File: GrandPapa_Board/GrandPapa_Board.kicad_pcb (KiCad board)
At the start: 2 copper layers, 82 x 82 mm, 0 parts

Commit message: add footprints, group layouts
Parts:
- added C1: 10uF, Capacitor_SMD:C_0805_2012Metric_Pad1.18x1.45mm_HandSolder, F.Cu at (253.8, 90.2)
- added C10: 4.7uF, Capacitor_SMD:C_0805_2012Metric_Pad1.18x1.45mm_HandSolder, F.Cu at (252.1, 25.6)
- added C11: 4.7uF, Capacitor_SMD:C_0805_2012Metric_Pad1.18x1.45mm_HandSolder, F.Cu at (260.4, 31.9)
- added C12: 0.1uF, Capacitor_SMD:C_0805_2012Metric_Pad1.18x1.45mm_HandSolder, F.Cu at (244.1, 21.0)
- added C13: 0.1uF, Capacitor_SMD:C_0805_2012Metric_Pad1.18x1.45mm_HandSolder, F.Cu at (60.6, 121.7)
- added C14: 0.1uF, Capacitor_SMD:C_0805_2012Metric_Pad1.18x1.45mm_HandSolder, F.Cu at (253.8, 77.5)
- added C15: 44 uF, Capacitor_SMD:C_0805_2012Metric_Pad1.18x1.45mm_HandSolder, F.Cu at (266.5, 94.0)
- added C16: 27pF, Capacitor_SMD:C_0805_2012Metric_Pad1.18x1.45mm_HandSolder, F.Cu at (155.8, 19.1)
- added C17: 27pF, Capacitor_SMD:C_0805_2012Metric_Pad1.18x1.45mm_HandSolder, F.Cu at (155.8, 24.0)
- added C18: 0.1uF 20V, Capacitor_SMD:C_0805_2012Metric_Pad1.18x1.45mm_HandSolder, F.Cu at (175.0, 24.8)
- added C19: 0.1uF 20V, Capacitor_SMD:C_0805_2012Metric_Pad1.18x1.45mm_HandSolder, F.Cu at (182.6, 34.7)
- added C2: 10uF, Capacitor_SMD:C_0805_2012Metric_Pad1.18x1.45mm_HandSolder, F.Cu at (41.0, 128.9)
- added C21: 0.1uF, Capacitor_SMD:C_0805_2012Metric_Pad1.18x1.45mm_HandSolder, F.Cu at (53.6, 34.9)
- added C22: 10uF, Capacitor_SMD:C_0805_2012Metric_Pad1.18x1.45mm_HandSolder, B.Cu at (25.4, 41.3)
- added C23: 10uF, Capacitor_SMD:C_0805_2012Metric_Pad1.18x1.45mm_HandSolder, F.Cu at (182.4, 31.1)
- added C3: 0.1uF, Capacitor_SMD:C_0805_2012Metric_Pad1.18x1.45mm_HandSolder, F.Cu at (253.8, 87.1)
- added C4: 5nF, Capacitor_SMD:C_0805_2012Metric_Pad1.18x1.45mm_HandSolder, F.Cu at (256.8, 103.5)
- added C5: 10uF, Capacitor_SMD:C_0805_2012Metric_Pad1.18x1.45mm_HandSolder, F.Cu at (44.5, 119.5)
- added C6: 0.1uF, Capacitor_SMD:C_0805_2012Metric_Pad1.18x1.45mm_HandSolder, F.Cu at (259.9, 94.0)
- added C7: 4.7uF, Capacitor_SMD:C_0805_2012Metric_Pad1.18x1.45mm_HandSolder, F.Cu at (50.5, 124.3)
- added C8: 25pF, Capacitor_SMD:C_0805_2012Metric_Pad1.18x1.45mm_HandSolder, F.Cu at (252.2, 103.6)
- added C9: 4.7uF, Capacitor_SMD:C_0805_2012Metric_Pad1.18x1.45mm_HandSolder, F.Cu at (255.3, 25.6)
- added D1: 150120BS75000, LED_SMD:LED_1206_3216Metric_Pad1.42x1.75mm_HandSolder, F.Cu at (240.6, 156.3)
- added D3: QBLP650-IW, LED_SMD:LED_1206_3216Metric_Pad1.42x1.75mm_HandSolder, F.Cu at (187.6, 44.5)
- added D4: 156120RS75000, LED_SMD:LED_1206_3216Metric_Pad1.42x1.75mm_HandSolder, F.Cu at (187.4, 40.6)
- added D5: 150120BS75000, LED_SMD:LED_1206_3216Metric_Pad1.42x1.75mm_HandSolder, F.Cu at (187.5, 36.8)
- added D6: QBLP650-IW, LED_SMD:LED_1206_3216Metric_Pad1.42x1.75mm_HandSolder, F.Cu at (250.8, 43.8)
- added D7: 156120RS75000, LED_SMD:LED_1206_3216Metric_Pad1.42x1.75mm_HandSolder, F.Cu at (253.4, 44.0)
- added D8: 150120BS75000, LED_SMD:LED_1206_3216Metric_Pad1.42x1.75mm_HandSolder, F.Cu at (248.3, 44.0)
- added F1: 1.2A, Fuse:Fuse_0805_2012Metric_Pad1.15x1.40mm_HandSolder, F.Cu at (248.0, 87.0)
- added F2: 1.2A, Fuse:Fuse_0805_2012Metric_Pad1.15x1.40mm_HandSolder, F.Cu at (27.6, 128.9)
- added F3: 1.2A, Fuse:Fuse_0805_2012Metric_Pad1.15x1.40mm_HandSolder, F.Cu at (260.4, 29.8)
- added H1: MountingHole_Pad, MountingHole:MountingHole_3.5mm_Pad_Via, F.Cu at (22.9, 165.1)
- added H2: MountingHole_Pad, MountingHole:MountingHole_3.5mm_Pad_Via, F.Cu at (36.8, 167.6)
- added H3: MountingHole_Pad, MountingHole:MountingHole_3.5mm_Pad_Via, F.Cu at (118.1, 137.2)
- added H4: MountingHole_Pad, MountingHole:MountingHole_3.5mm_Pad_Via, F.Cu at (40.6, 186.1)
- added H5: MountingHole_Pad, MountingHole:MountingHole_3.5mm_Pad_Via, F.Cu at (24.1, 177.8)
- added H6: MountingHole_Pad, MountingHole:MountingHole_3.5mm_Pad_Via, F.Cu at (190.5, 65.4)
- added H7: MountingHole_Pad, MountingHole:MountingHole_3.5mm_Pad_Via, F.Cu at (190.5, 137.8)
- added H8: MountingHole_Pad, MountingHole:MountingHole_3.5mm_Pad_Via, F.Cu at (118.1, 64.8)
- added J1: 3.7V LiPo Single Cell, Connector_JST:JST_PH_S2B-PH-K_1x02_P2.00mm_Horizontal, F.Cu at (266.8, 31.5)
- added J11: Dupont 01x04_Male, Connector_PinHeader_2.54mm:PinHeader_1x04_P2.54mm_Vertical, F.Cu at (54.0, 174.6)
- added J2: HARWIN_ROCKET, PapaOld:connector_Harwin_M80-5000642, F.Cu at (196.6, 29.8)
- added J3: Dupont 02x03_Female, PapaOld:PinHeader_2x03_P2.00mm_Vertical_MINISENSOR_Harwin_Spacing, F.Cu at (120.0, 82.5)
- added J4: HARWIN_MINISENSOR, PapaOld:connector_Harwin_M80-5000642, F.Cu at (43.1, 26.7)
- added J5: Dupont 01x06_Female, PapaOld:PinHeader_2x03_P2.00mm_Vertical_MINISENSOR_Harwin_Spacing, F.Cu at (181.3, 115.6)
- added J6: Conn_02x06, Connector_PinHeader_2.54mm:PinHeader_1x05_P2.54mm_Vertical, F.Cu at (182.2, 21.0)
- added J7: HARWIN_KALMAN, PapaOld:connector_Harwin_M80-5000642, F.Cu at (42.9, 32.4)
- added L1: 5.6uH, Inductor_SMD:L_Vishay_IHLP-2020, F.Cu at (263.4, 99.1)
- added L2: 4.7uH, Inductor_SMD:L_Sumida_CDMC6D28_7.25x6.5mm, F.Cu at (33.0, 123.2)
- added R1: 20mR, Resistor_SMD:R_1206_3216Metric_Pad1.30x1.75mm_HandSolder, F.Cu at (248.2, 84.5)
- added R10: 0, Resistor_SMD:R_0805_2012Metric_Pad1.20x1.40mm_HandSolder, F.Cu at (50.4, 121.9)
- added R11: 10kR, Resistor_SMD:R_0805_2012Metric_Pad1.20x1.40mm_HandSolder, F.Cu at (168.0, 19.7)
- added R12: 100R, Resistor_SMD:R_0805_2012Metric_Pad1.20x1.40mm_HandSolder, F.Cu at (167.0, 24.1)
- added R13: 100R, Resistor_SMD:R_0805_2012Metric_Pad1.20x1.40mm_HandSolder, F.Cu at (182.4, 44.5)
- added R14: 150R, Resistor_SMD:R_0805_2012Metric_Pad1.20x1.40mm_HandSolder, F.Cu at (182.3, 40.6)
- added R15: 100R, Resistor_SMD:R_0805_2012Metric_Pad1.20x1.40mm_HandSolder, F.Cu at (182.6, 36.8)
- added R16: 11kR, Resistor_SMD:R_0805_2012Metric_Pad1.20x1.40mm_HandSolder, F.Cu at (256.9, 106.0)
- added R17: 10kR, Resistor_SMD:R_0805_2012Metric_Pad1.20x1.40mm_HandSolder, F.Cu at (53.6, 40.0)
- added R18: 10kR, Resistor_SMD:R_0805_2012Metric_Pad1.20x1.40mm_HandSolder, F.Cu at (53.6, 37.5)
- added R19: 70kR, Resistor_SMD:R_0805_2012Metric_Pad1.20x1.40mm_HandSolder, F.Cu at (248.3, 99.1)
- added R2: 1MR, Resistor_SMD:R_0805_2012Metric_Pad1.20x1.40mm_HandSolder, F.Cu at (47.0, 122.8)
- added R20: 470R, Resistor_SMD:R_0805_2012Metric_Pad1.20x1.40mm_HandSolder, F.Cu at (253.4, 37.2)
- added R21: 470R, Resistor_SMD:R_0805_2012Metric_Pad1.20x1.40mm_HandSolder, F.Cu at (248.3, 37.2)
- added R22: 0, Resistor_SMD:R_0805_2012Metric_Pad1.20x1.40mm_HandSolder, F.Cu at (248.6, 29.2)
- added R23: 20mR, Resistor_SMD:R_1206_3216Metric_Pad1.30x1.75mm_HandSolder, F.Cu at (243.6, 29.2)
- added R24: 0, Resistor_SMD:R_0805_2012Metric_Pad1.20x1.40mm_HandSolder, F.Cu at (248.6, 26.7)
- added R25: 324kR, Resistor_SMD:R_0805_2012Metric_Pad1.20x1.40mm_HandSolder, F.Cu at (252.2, 106.0)
- added R26: 10kR, Resistor_SMD:R_0805_2012Metric_Pad1.20x1.40mm_HandSolder, F.Cu at (36.7, 45.1)
- added R27: 15k, Resistor_SMD:R_0805_2012Metric_Pad1.20x1.40mm_HandSolder, F.Cu at (259.3, 84.5)
- added R3: 100R, Resistor_SMD:R_0805_2012Metric_Pad1.20x1.40mm_HandSolder, F.Cu at (245.4, 156.2)
- added R4: 2kR, Resistor_SMD:R_0805_2012Metric_Pad1.20x1.40mm_HandSolder, F.Cu at (258.4, 37.1)
- added R5: 25kR, Resistor_SMD:R_0805_2012Metric_Pad1.20x1.40mm_HandSolder, F.Cu at (255.9, 37.1)
- added R6: 470R, Resistor_SMD:R_0805_2012Metric_Pad1.20x1.40mm_HandSolder, F.Cu at (250.8, 37.2)
- added R7: 500R, Resistor_SMD:R_0805_2012Metric_Pad1.20x1.40mm_HandSolder, F.Cu at (60.6, 123.8)
- added R8: 10k, Resistor_SMD:R_0805_2012Metric_Pad1.20x1.40mm_HandSolder, F.Cu at (259.4, 87.6)
- added R9: 0, Resistor_SMD:R_0805_2012Metric_Pad1.20x1.40mm_HandSolder, F.Cu at (253.8, 84.5)
- added TH1: 10k, Resistor_SMD:R_0805_2012Metric_Pad1.20x1.40mm_HandSolder, F.Cu at (248.6, 33.7)
- added TP1: TestPoint, Connector_PinHeader_2.54mm:PinHeader_1x01_P2.54mm_Vertical, F.Cu at (258.4, 45.1)
- added TP2: TestPoint, Connector_PinHeader_2.54mm:PinHeader_1x01_P2.54mm_Vertical, F.Cu at (238.1, 21.3)
- added TP3: TestPoint, Connector_PinHeader_2.54mm:PinHeader_1x01_P2.54mm_Vertical, F.Cu at (55.9, 128.3)
- added TP4: TestPoint, Connector_PinHeader_2.54mm:PinHeader_1x01_P2.54mm_Vertical, F.Cu at (259.5, 75.6)
- added TP5: TestPoint, Connector_PinHeader_2.54mm:PinHeader_1x01_P2.54mm_Vertical, F.Cu at (248.9, 19.7)
- added TP6: TestPoint, Connector_PinHeader_2.54mm:PinHeader_1x01_P2.54mm_Vertical, F.Cu at (22.2, 128.9)
- added TP7: TestPoint, Connector_PinHeader_2.54mm:PinHeader_1x01_P2.54mm_Vertical, F.Cu at (190.5, 17.1)
- added U1: MCP1642B-50I/MS, Package_SO:MSOP-8_3x3mm_P0.65mm, F.Cu at (41.2, 122.9)
- added U10: MCP2515-I/P, Package_SO:SOIC-18W_7.5x11.6mm_P1.27mm, F.Cu at (45.1, 42.5)
- added U2: BD9E302EFJ, Package_SO:HTSOP-8-1EP_3.9x4.9mm_P1.27mm_EP2.4x3.2mm, F.Cu at (254.3, 96.6)
- added U3: MCP73871T-1CCI/ML, Package_DFN_QFN:QFN-20-1EP_4x4mm_P0.5mm_EP2.5x2.5mm, F.Cu at (254.0, 31.1)
- added U4: INA180, Package_TO_SOT_SMD:SOT-23-5_HandSoldering, F.Cu at (243.9, 26.0)
- added U5: FPF2124, Package_TO_SOT_SMD:SOT-23-5_HandSoldering, F.Cu at (55.5, 122.8)
- added U6: INA180, Package_TO_SOT_SMD:SOT-23-5_HandSoldering, F.Cu at (248.4, 78.5)
- added U7: MCP2562-E/SN, Package_SO:SOIC-8_3.9x4.9mm_P1.27mm, B.Cu at (31.5, 39.4)
- added U8: MCP2562-E/SN, Package_SO:SOIC-8_3.9x4.9mm_P1.27mm, F.Cu at (189.2, 30.5)
- added U9: PIC18F26K83, Package_SO:SSOP-28_5.3x10.2mm_P0.65mm, F.Cu at (172.7, 33.0)
- added Y1: 12MHz, Crystal:Crystal_HC49-4H_Vertical, F.Cu at (160.7, 19.1)
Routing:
- net Net-(C2-Pad1): track 0.00 -> 29.8 mm
- net Net-(C16-Pad1): track 0.00 -> 26.1 mm
- net Net-(C17-Pad1): track 0.00 -> 21.5 mm
- net /MCU and CAN Controllers/~{MCLR}: track 0.00 -> 13.2 mm
- net +5V: track 0.00 -> 12.5 mm
- net Net-(C1-Pad1): track 0.00 -> 12.3 mm
- net /MCU and CAN Controllers/ICSPCLK: track 0.00 -> 12.0 mm
- net Net-(L2-Pad2): track 0.00 -> 11.7 mm
- net Net-(R13-Pad1): track 0.00 -> 11.6 mm
- net /MCU and CAN Controllers/ICSPDAT: track 0.00 -> 10.4 mm
- net Net-(C6-Pad1): track 0.00 -> 9.93 mm
- net Net-(R1-Pad1): track 0.00 -> 8.16 mm
- net Net-(R14-Pad1): track 0.00 -> 8.08 mm
- net /Battery Charging/VBATT_VOLT_SENSE: track 0.00 -> 7.42 mm
- net Net-(C10-Pad1): track 0.00 -> 7.40 mm
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
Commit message: change stackup, mounting holes, connector footprints, power reg layout, fuse values
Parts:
- J2, J7: moved to B.Cu
- J3, J5: footprint PapaOld:PinHeader_2x03_P2.00mm_Vertical_MINISENSOR_Harwin_Spacing -> PapaOld:connector_Harwin_M80-5000642
- R27: value 15k -> 15kR
- R8: value 10k -> 10kR
- moved TP4 237.3 mm to (37.9, 160.5)
- moved R8 231.7 mm to (42.5, 169.1)
- moved R27 231.4 mm to (42.5, 165.7), turned to 180 degrees
- moved C8 229.5 mm to (39.7, 190.3), turned to 90 degrees
- moved R16 226.4 mm to (45.2, 186.3), turned to 90 degrees
- moved L1 226.3 mm to (53.4, 183.5)
- moved C4 225.6 mm to (45.2, 181.7), turned to 90 degrees
- moved R19 225.2 mm to (42.4, 190.3), turned to -90 degrees
- moved R25 225.2 mm to (41.5, 185.4)
- moved C15 225.1 mm to (59.5, 182.4), turned to 90 degrees
- moved C6 225.0 mm to (51.0, 177.3), turned to 90 degrees
- moved U2 223.0 mm to (45.8, 175.6)
- moved C3 222.1 mm to (47.4, 169.2), turned to 0 degrees
- moved R9 221.7 mm to (45.2, 159.5), turned to -90 degrees
- moved C1 219.9 mm to (47.3, 165.7), turned to 0 degrees
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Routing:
- net Net-(C2-Pad1): track 29.8 -> 0.00 mm
- net Net-(C16-Pad1): track 26.1 -> 10.4 mm
- net Net-(C1-Pad1): track 12.3 -> 0.00 mm
- net Net-(L2-Pad2): track 11.7 -> 0.00 mm
- net Net-(R13-Pad1): track 11.6 -> 0.00 mm
- net Net-(C17-Pad1): track 21.5 -> 10.4 mm
- net Net-(C6-Pad1): track 9.93 -> 0.00 mm
- net Net-(R14-Pad1): track 8.08 -> 0.00 mm
- net Net-(R4-Pad1): track 6.38 -> 0.60 mm
- net Net-(R5-Pad1): track 5.80 -> 0.46 mm
- net Net-(C7-Pad1): track 5.17 -> 0.00 mm
- net Net-(R15-Pad1): track 5.93 -> 1.12 mm
- net +5V: track 12.5 -> 8.11 mm
- net Net-(R23-Pad1): track 0.00 -> 4.24 mm
- net Net-(R22-Pad2): track 0.00 -> 4.22 mm
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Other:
- outline, holes or cut-outs redrawn
- copper layers 2 -> 4
- board text added: "5V_ALWAYS"
- board text added: "GPS"
- board text added: "KALMAN"
- board text added: "LOGGER"
- board text added: "MINISENSOR"
- board text added: "ROCKETCAN"

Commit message: 4 straight hours of traces
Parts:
- removed TP6: TestPoint, Connector_PinHeader_2.54mm:PinHeader_1x01_P2.54mm_Vertical
- C12, C13, C2, C21, C5, C7, F2, J1, R10, R17, R18, R2, R23, R24, R26, R7, TH1, U1, U10, U4, U5: moved to B.Cu
- C22, J7, U7: moved to F.Cu
- F1, F3: value 1.2A -> 1.5A
- moved J1 138.8 mm to (171.8, 132.8)
- moved C22 132.1 mm to (193.7, 102.0), turned to -90 degrees
- moved TP1 129.0 mm to (147.9, 111.7)
- moved F2 126.7 mm to (157.3, 134.1), turned to 180 degrees
- moved TP4 126.5 mm to (147.4, 97.2)
- moved L1 124.5 mm to (150.0, 104.8)
- moved U7 121.0 mm to (188.7, 97.3), turned to 0 degrees
- moved C3 120.1 mm to (139.6, 92.1)
- moved C1 119.8 mm to (139.6, 89.3)
- moved C2 119.0 mm to (153.4, 133.1)
- moved R19 118.6 mm to (132.7, 113.5)
- moved C6 118.2 mm to (141.2, 101.0)
- moved R27 118.2 mm to (132.8, 89.4)
- moved R8 118.2 mm to (132.7, 92.8)
- moved U2 118.2 mm to (136.0, 99.3)
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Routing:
- net /Power Supplies & Regulators/5V_SWITCHED: track 0.00 -> 205.5 mm
- net /CANH_PAYLOAD: track 0.00 -> 166.3 mm
- net /CANL_PAYLOAD: track 0.00 -> 156.4 mm
- net /Battery Charging/BATT_CHARGER_PG: track 0.00 -> 86.7 mm, vias 0 -> 2
- net /MCU and CAN Controllers/CANH_ROCKET: track 0.00 -> 79.5 mm, vias 0 -> 1
- net +5V: track 8.11 -> 86.2 mm, vias 0 -> 11
- net /Battery Charging/VBATT_CURR_SENSE: track 0.00 -> 74.4 mm, vias 0 -> 1
- net /Battery Charging/BATT_CHARGE_COMPLETE: track 0.00 -> 73.8 mm, vias 0 -> 2
- net /MCU and CAN Controllers/CANL_ROCKET: track 0.00 -> 73.1 mm, vias 0 -> 1
- net /Battery Charging/LOW_BAT: track 0.00 -> 69.4 mm, vias 0 -> 2
- net /MCU and CAN Controllers/12V_PWR_DIS: track 0.00 -> 64.7 mm, vias 0 -> 2
- net +BATT: track 0.00 -> 63.8 mm
- net +4.5V: track 0.00 -> 58.6 mm, vias 0 -> 6
- net /Battery Charging/VBATT_VOLT_SENSE: track 7.42 -> 63.2 mm, vias 0 -> 2
- net GND: track 0.00 -> 55.4 mm, vias 0 -> 8
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- added copper zone on In1.Cu, net +4.5V
- added copper zone on In1.Cu, net +5V
- added copper zone on B.Cu, net GND
- added copper zone on F.Cu, net GND
- added copper zone on In2.Cu, net GND

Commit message: update layout + routing
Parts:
- C1, C10, C11, C14, C15, C3, C4, C6, C8, C9, F1, F3, L1, L2, R1, R16, R19, R22, R25, R27, R4, R5, R8, R9, TP1, TP3, TP4, TP5, U2, U3, U6: moved to B.Cu
- moved R7 68.9 mm to (183.7, 118.3), turned to 0 degrees
- moved C13 63.5 mm to (176.0, 117.2), turned to 90 degrees
- moved U5 62.6 mm to (179.5, 116.9), turned to -90 degrees
- moved C7 56.2 mm to (179.6, 112.6), turned to 0 degrees
- moved F2 48.1 mm to (183.6, 93.8), turned to -90 degrees
- moved TP3 47.8 mm to (167.8, 105.6), turned to 180 degrees
- moved R10 47.3 mm to (170.8, 108.3), turned to -90 degrees
- moved C2 41.2 mm to (178.5, 100.4), turned to -90 degrees
- moved L2 39.6 mm to (175.8, 94.4)
- moved R2 39.5 mm to (174.2, 107.4)
- moved C5 39.2 mm to (170.9, 102.7)
- moved U1 39.2 mm to (174.7, 101.6)
- moved C10 29.5 mm to (148.2, 122.3), turned to -90 degrees
- moved TP4 27.2 mm to (140.5, 70.9), turned to 180 degrees
- moved F3 24.4 mm to (158.6, 119.3)
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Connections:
- J2 pad 4: /MCU and CAN Controllers/CANL_ROCKET -> /MCU and CAN Controllers/CANH_ROCKET
- J2 pad 5: /MCU and CAN Controllers/CANH_ROCKET -> /MCU and CAN Controllers/CANL_ROCKET
- J4 pad 4: /CANL_PAYLOAD -> /CANH_PAYLOAD
- J4 pad 5: /CANH_PAYLOAD -> /CANL_PAYLOAD
- J7 pad 4: /CANL_PAYLOAD -> /CANH_PAYLOAD
- J7 pad 5: /CANH_PAYLOAD -> /CANL_PAYLOAD
- TP3 pad 1: Net-(C7-Pad1) -> +5V
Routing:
- net /Power Supplies & Regulators/5V_SWITCHED: track 205.5 -> 0.02 mm, vias 0 -> 4
- net +5V: track 86.2 -> 40.8 mm, vias 11 -> 15
- net Net-(TH1-Pad1): track 3.28 -> 43.3 mm, vias 1 -> 2
- net /MCU and CAN Controllers/AUX_PWR_EN: track 18.0 -> 57.9 mm, vias 1 -> 3
- net /MCU and CAN Controllers/CANH_ROCKET: track 79.5 -> 45.5 mm
- net /Battery Charging/VBATT_CURR_SENSE: track 74.4 -> 40.9 mm, vias 1 -> 3
- net /CANL_PAYLOAD: track 156.4 -> 185.9 mm, vias 0 -> 5
- net +BATT: track 63.8 -> 37.0 mm, vias 0 -> 2
- net /MCU and CAN Controllers/CANL_ROCKET: track 73.1 -> 46.3 mm
- net Net-(F3-Pad1): track 37.2 -> 11.4 mm, vias 1 -> 0
- net Net-(C1-Pad1): track 44.4 -> 19.8 mm, vias 1 -> 0
- net /CANH_PAYLOAD: track 166.3 -> 189.4 mm, vias 0 -> 5
- net /MCU and CAN Controllers/12V_PWR_DIS: track 64.7 -> 45.2 mm, vias 2 -> 3
- net +12V: track 16.1 -> 0.00 mm
- net /MCU and CAN Controllers/CAN_INT: track 43.3 -> 27.3 mm, vias 1 -> 3
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- added copper zone on B.Cu, net +12V
- added copper zone on B.Cu, net +4.5V
- added copper zone on B.Cu, net +5V
- added copper zone on B.Cu, net /Battery Charging/VBATT_VOLT_SENSE
- added copper zone on B.Cu, net /Power Supplies & Regulators/5V_SWITCHED
- added copper zone on In1.Cu, net /Power Supplies & Regulators/5V_SWITCHED
- added copper zone on B.Cu, net Net-(C1-Pad1)
- added copper zone on B.Cu, net Net-(C2-Pad1)
- added copper zone on B.Cu, net Net-(C6-Pad1)
- added copper zone on B.Cu, net Net-(L2-Pad2)
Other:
- outline, holes or cut-outs redrawn
- board text removed: "5V_ALWAYS"

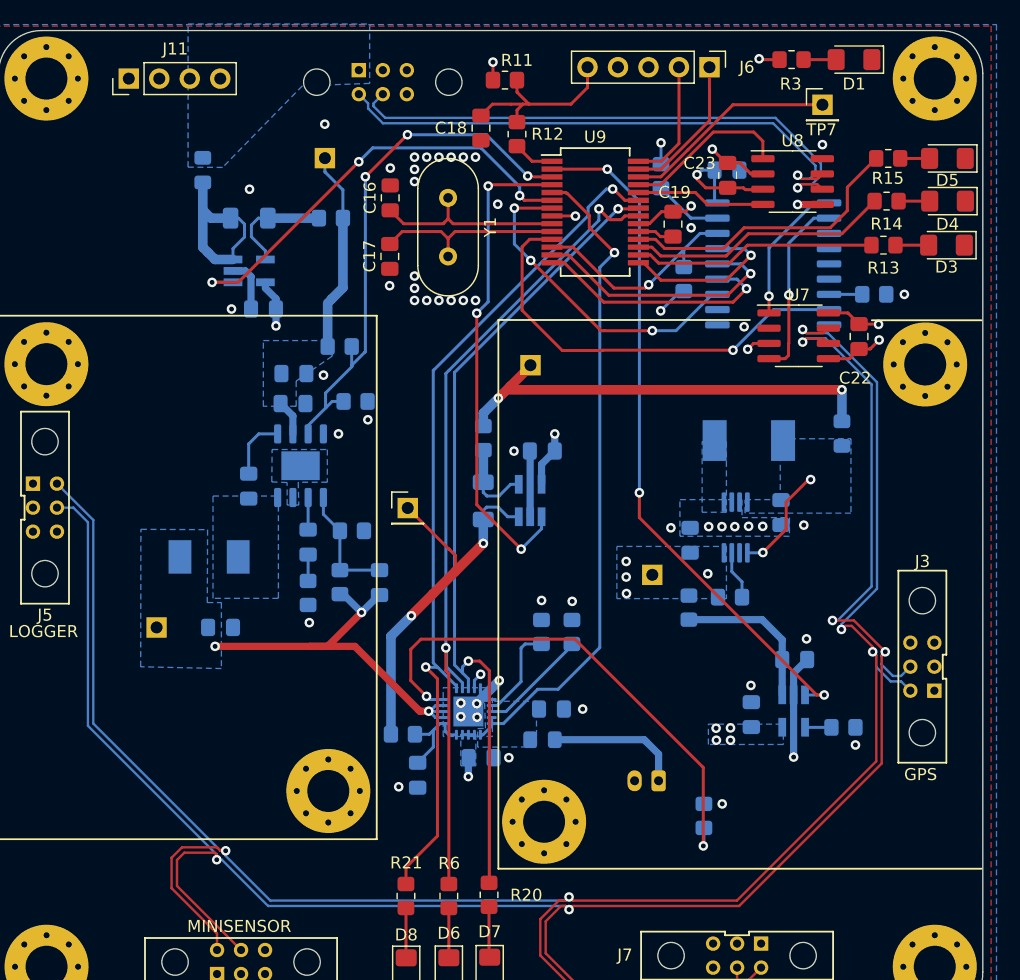
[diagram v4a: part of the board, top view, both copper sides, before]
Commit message: Fix silkscreen; add logo
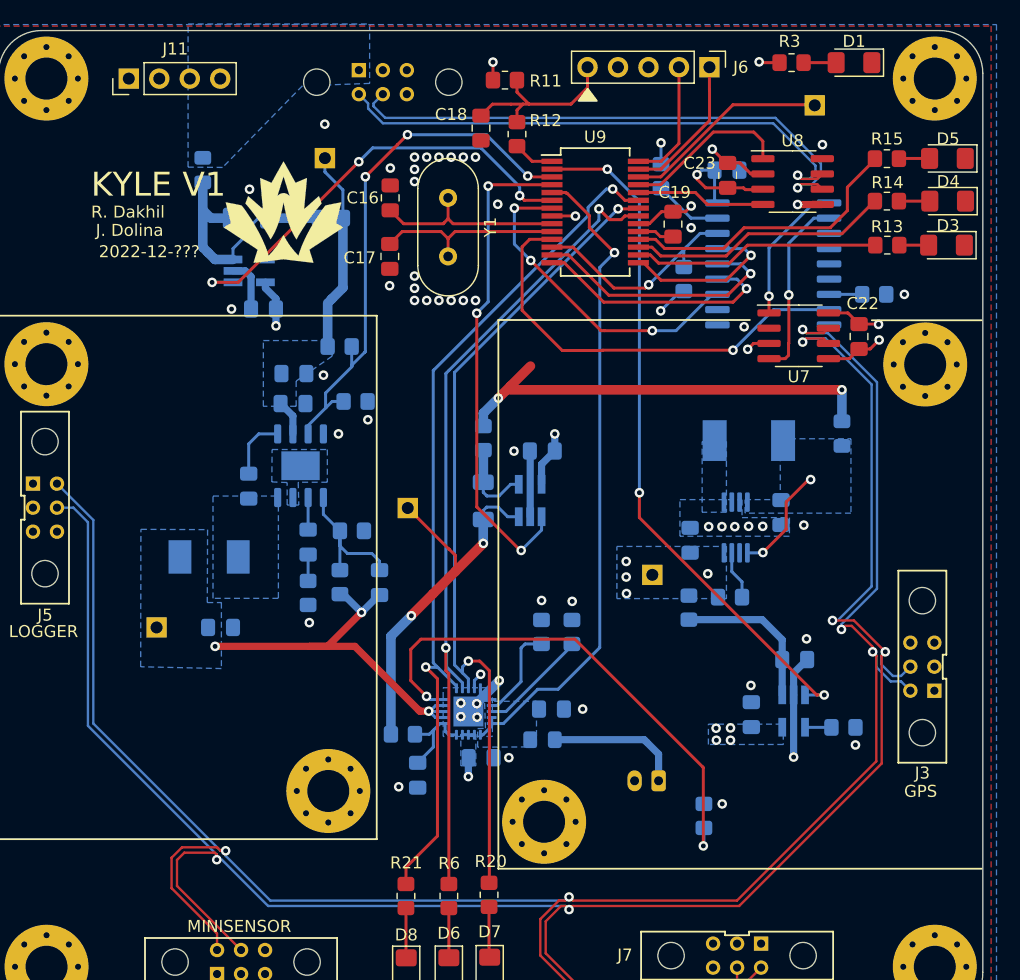
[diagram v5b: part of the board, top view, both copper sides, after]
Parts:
- removed TP5: TestPoint, Connector_PinHeader_2.54mm:PinHeader_1x01_P2.54mm_Vertical
- added G***: LOGO, GrandPapa:Logo_SilkScreen_10mm, F.Cu at (137.0, 75.4)
- J3: value Dupont 02x03_Female -> Dupont_GPS
- J5: value Dupont 01x06_Female -> Dupont_Logger
- TP2, TP7: moved to B.Cu
- moved TP7 0.64 mm to (181.3, 66.5), turned to 180 degrees
- moved R13 0.32 mm to (187.3, 78.1)
- moved D1 0.25 mm to (184.6, 62.9)
- moved R3 0.25 mm to (179.4, 62.9)
- moved R15 0.11 mm to (187.3, 70.9)
- turned TP2 to 180 degrees
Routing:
- net Net-(C8-Pad2): track 9.92 -> 12.5 mm
- net GND: vias 56 -> 55
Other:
- board text added: "+12V"
- board text added: "+4.5V"
- board text added: "+5V"
- board text added: "+BATT"
- board text added: "2022-12-???"
- board text added: "J. Dolina"
- board text added: "KYLE V1"
- board text added: "PIN 26"
- board text added: "R. Dakhil"

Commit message: Fix DRC errors
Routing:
- net +BATT: track 37.0 -> 34.4 mm
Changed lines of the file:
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@@
     (property "Sheetname" "")
     (attr through_hole)
-    (fp_text reference "J7" (at 9.3472 0.0508) (layer "F.SilkS")
+    (fp_text reference "J7" (at -0.3048 -3.0734) (layer "F.SilkS")
       (effects (font (size 1 1) (thickness 0.15)))
     )
@@
     (property "Sheetname" "Battery Charging")
     (attr smd)
-    (fp_text reference "R20" (at -2.783 -0.141) (layer "F.SilkS")
+    (fp_text reference "R20" (at 0.011 -2.681) (layer "F.SilkS")
       (effects (font (size 1 1) (thickness 0.15)))
     )
@@
     (effects (font (size 1 1) (thickness 0.15)) (justify mirror))
   )
-  (gr_text "KALMAN" (at 174.5996 140.5382) (layer "F.SilkS")
+  (gr_text "KALMAN" (at 174.8282 134.0358) (layer "F.SilkS")
     (effects (font (size 1 1) (thickness 0.25)))
   )
@@
   (segment (start 152.444 116.9768) (end 152.5162 116.9768) (width 0.25) (layer "B.Cu") (net 2))
   (segment (start 153.139 116.3218) (end 153.139 116.3118) (width 0.25) (layer "B.Cu") (net 2))
+  (segment (start 132.8306 80.266) (end 133.8606 80.266) (width 0.6) (layer "B.Cu") (net 2))
   (segment (start 179.537762 115.585992) (end 179.537762 120.770562) (width 0.6) (layer "B.Cu") (net 2))
   (segment (start 155.009 114.3918) (end 155.009 114.4118) (width 0.25) (layer "B.Cu") (net 2))
@@
   (segment (start 153.444 115.9768) (end 152.444 116.9768) (width 0.25) (layer "B.Cu") (net 2))
   (segment (start 154.3815 115.9768) (end 153.444 115.9768) (width 0.25) (layer "B.Cu") (net 2))
-  (segment (start 134.334 80.7394) (end 134.334 83.4418) (width 0.6) (layer "B.Cu") (net 2))
-  (segment (start 132.8306 80.266) (end 133.8606 80.266) (width 0.6) (layer "B.Cu") (net 2))
+  (segment (start 134.251089 80.656489) (end 134.251089 81.9576) (width 0.6) (layer "B.Cu") (net 2))
   (segment (start 155.009 114.4118) (end 152.444 116.9768) (width 0.8) (layer "B.Cu") (net 2))
   (segment (start 152.5162 116.9768) (end 153.2426 116.2504) (width 0.25) (layer "B.Cu") (net 2))
+  (segment (start 134.251089 81.9576) (end 134.334 82.040511) (width 0.6) (layer "B.Cu") (net 2))
+  (segment (start 133.8606 80.266) (end 134.251089 80.656489) (width 0.6) (layer "B.Cu") (net 2))
   (segment (start 139.1602 108.5055) (end 139.1982 108.5435) (width 0.25) (layer "B.Cu") (net 2))
   (segment (start 179.537762 115.585992) (end 179.537762 113.773038) (width 0.6) (layer "B.Cu") (net 2))
   (segment (start 153.444 115.0393) (end 153.444 115.9768) (width 0.25) (layer "B.Cu") (net 2))
   (segment (start 157.589 95.2968) (end 157.589 100.7468) (width 0.6) (layer "B.Cu") (net 2))
-  (segment (start 133.8606 80.266) (end 134.334 80.7394) (width 0.6) (layer "B.Cu") (net 2))
   (segment (start 179.537762 113.773038) (end 180.664 112.6468) (width 0.6) (layer "B.Cu") (net 2))
+  (segment (start 134.334 82.040511) (end 134.334 83.4418) (width 0.6) (layer "B.Cu") (net 2))
   (segment (start 176.979 103.7318) (end 178.919 101.7918) (width 0.25) (layer "F.Cu") (net 3))
   (segment (start 178.919 99.5218) (end 180.789 97.6518) (width 0.25) (layer "F.Cu") (net 3))
@@
   (segment (start 133.789 76.3718) (end 133.789 77.4468) (width 0.25) (layer "B.Cu") (net 26))
   (segment (start 133.289 75.8718) (end 133.789 76.3718) (width 0.25) (layer "B.Cu") (net 26))
-  (segment (start 155.939 89.8718) (end 154.939 90.8718) (width 0.8) (layer "F.Cu") (net 27))
-  (segment (start 155.939 89.8718) (end 157.614 88.1968) (width 0.8) (layer "F.Cu") (net 27))
-  (segment (start 183.5615 90.1718) (end 155.9365 90.1718) (width 0.8) (layer "F.Cu") (net 27))
-  (segment (start 157.614 88.1968) (end 157.614 88.1218) (width 0.25) (layer "F.Cu") (net 27))
+  (segment (start 183.5615 90.1718) (end 155.639 90.1718) (width 0.8) (layer "F.Cu") (net 27))
+  (segment (start 155.639 90.1718) (end 154.939 90.8718) (width 0.8) (layer "F.Cu") (net 27))
   (via (at 183.559 90.1718) (size 0.8) (drill 0.4) (layers "F.Cu" "B.Cu") (net 27))
   (via (at 154.939 90.8718) (size 0.8) (drill 0.4) (layers "F.Cu" "B.Cu") (net 27))
@@
     (polygon
       (pts
-        (xy 136.614 107.5468)
-        (xy 131.164 107.5468)
+        (xy 136.614 107.2928)
+        (xy 131.164 107.2928)
         (xy 131.164 99.0218)
         (xy 136.614 99.0218)
@@
     (polygon
       (pts
-        (xy 131.864 113.3968)
-        (xy 125.139 113.2468)
+        (xy 131.953 113.3968)
+        (xy 125.095 113.2468)
         (xy 125.159049 101.796758)
-        (xy 130.713586 101.822417)
-        (xy 130.688586 107.897417)
+        (xy 130.45959 101.821371)
+        (xy 130.43459 107.896371)
         (xy 131.864 107.8968)
       )
